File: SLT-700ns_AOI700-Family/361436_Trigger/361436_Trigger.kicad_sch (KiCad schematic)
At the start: 23 parts, among them T1 AAA, T2 CB, T3 CB, T4 AAA, U1 16-Pin_SLx_Can

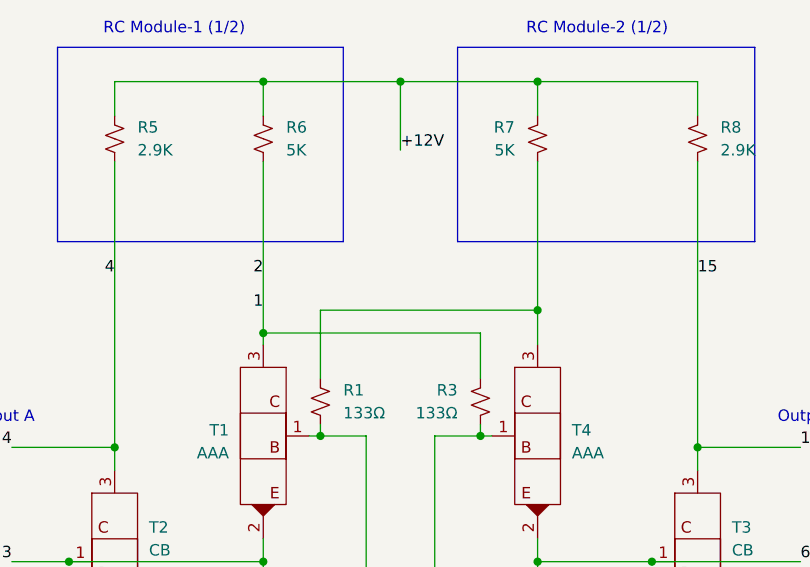
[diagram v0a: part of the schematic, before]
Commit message: Add can P/N to schematics for SLT-700
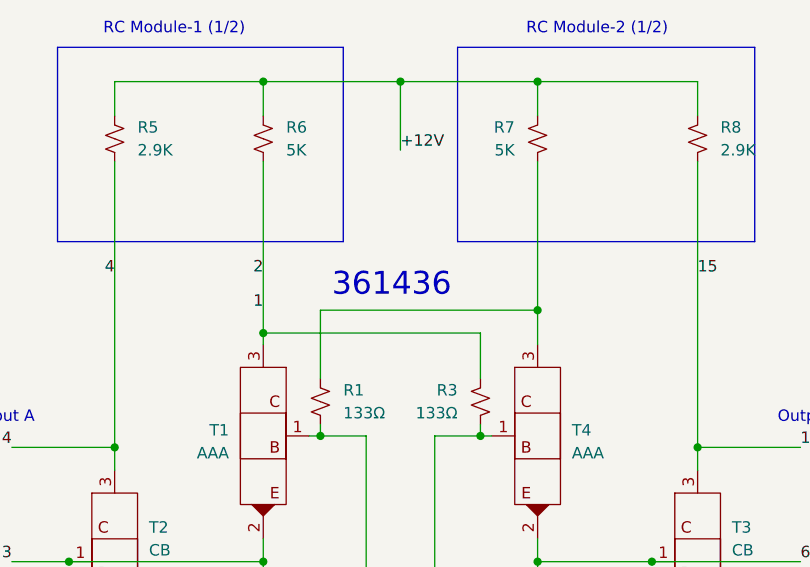
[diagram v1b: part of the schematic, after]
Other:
- note added: "361436"
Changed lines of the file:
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@@
     (effects (font (size 1.27 1.27)) (justify right bottom))
+  )
+  (text "361436" (at 83.82 60.96 0)
+    (effects (font (size 2.54 2.54)) (justify left bottom))
   )
   (text "Output B" (at 133.35 74.93 0)
